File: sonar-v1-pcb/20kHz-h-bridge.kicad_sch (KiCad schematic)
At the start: 1 part, among them U5 DRV8876PWPR

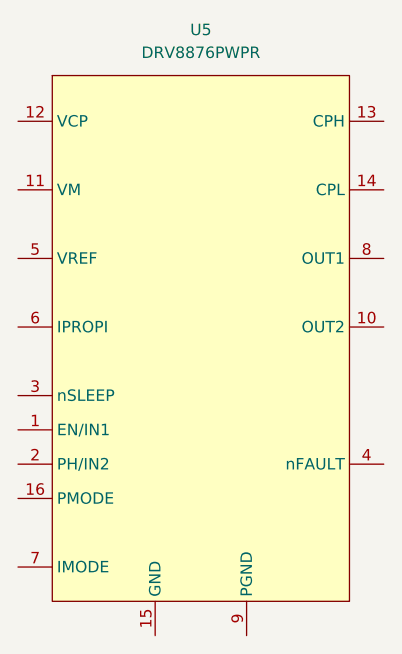
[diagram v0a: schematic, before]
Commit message: WIP hand-off: rx amp sim project, SPICE models, schematic updates
Adds rx_amp_sim KiCad project, SPICE models, Python setup-kicad.py
(replaces test_py.sh), CLAUDE.md, and a sweep of schematic edits across
the v1 board.

Co-Authored-By: Claude Opus 4.7 <noreply@anthropic.com>
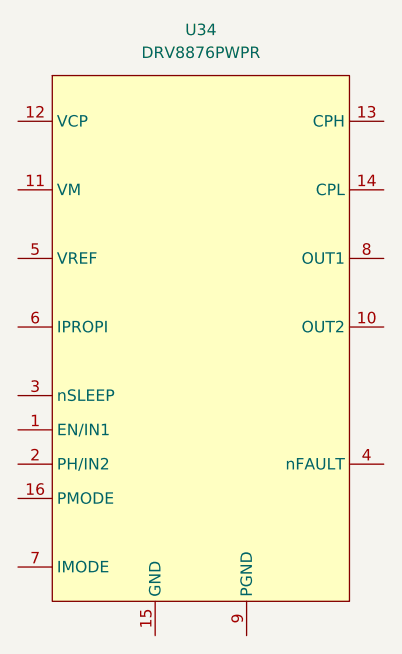
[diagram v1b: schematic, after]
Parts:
- renumbered U5 to U34
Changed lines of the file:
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@@
 		(dnp no)
 		(fields_autoplaced yes)
-		(property "Reference" "U5"
+		(property "Reference" "U34"
 			(at 148.59 69.85 0)
 			(show_name no)
@@
 			(project "sonar"
 				(path "/f72ceae0-eee4-4385-b0e8-639846bcb5f2/c6a046af-5387-4c6b-a77e-149ae78eccdc"
-					(reference "U5")
+					(reference "U34")
 					(unit 1)
 				)
